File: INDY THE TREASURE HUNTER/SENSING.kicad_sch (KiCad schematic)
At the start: 1 part

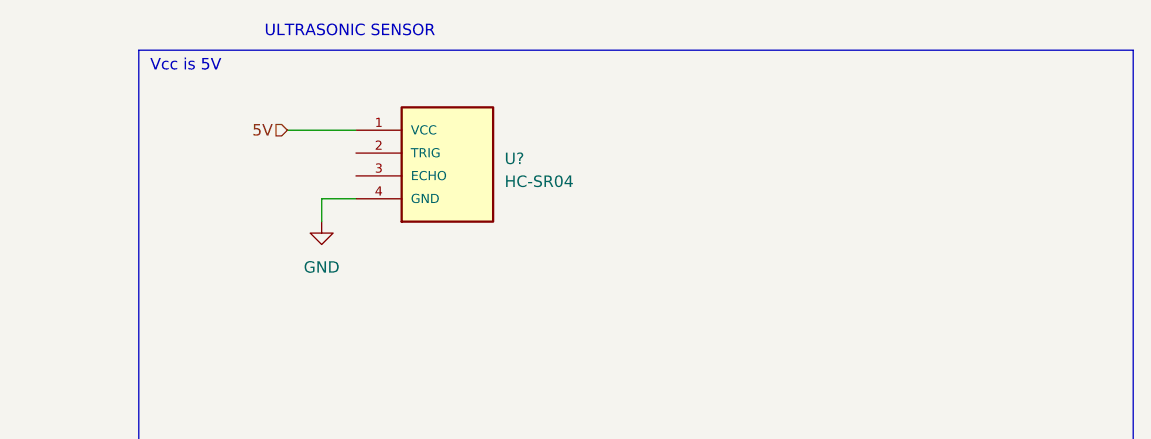
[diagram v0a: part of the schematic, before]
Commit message: 19:16
Got rid of the boxes around the logic level converters, we can neaten those up later it was just becoming a nightmare.

Also IMPORTANT:
Try to stick with this naming convention for logic level lines: NAMEOFLINE_VOLTAGE (eg: ULTRA_TRIG_3V3) so we can track the logic level voltages
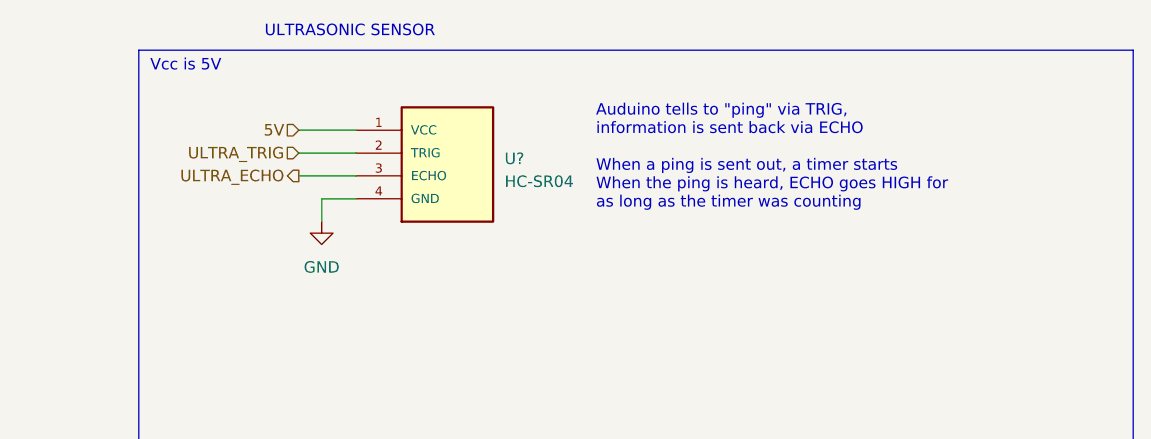
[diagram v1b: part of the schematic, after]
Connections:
- net ULTRA_TRIG: now reaches U?.2 (TRIG)
- net ULTRA_ECHO: now reaches U?.3 (ECHO)
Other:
- note added: "Auduino tells to "ping" via TRIG, information is sent back via ECHO When a ping is sent out, a timer starts When the ping is heard, ECHO goes HIGH for as long as the timer was counting"
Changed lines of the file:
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@@
 (kicad_sch (version 20230121) (generator eeschema)
   (paper "A4")
-  (wire (pts (xy 182.88 49.53) (xy 190.5 49.53))
+  (wire (pts (xy 184.15 54.61) (xy 190.5 54.61))
     (stroke (width 0) (type default))
   )
   (wire (pts (xy 190.5 57.15) (xy 186.69 57.15))
+    (stroke (width 0) (type default))
+  )
+  (wire (pts (xy 184.15 52.07) (xy 190.5 52.07))
+    (stroke (width 0) (type default))
+  )
+  (wire (pts (xy 184.15 49.53) (xy 190.5 49.53))
     (stroke (width 0) (type default))
   )
@@
     (effects (font (size 1.27 1.27)) (justify left bottom))
   )
-  (hierarchical_label "5V" (shape input) (at 182.88 49.53 180) (fields_autoplaced)
+  (text "Auduino tells to \"ping\" via TRIG,\ninformation is sent back via ECHO\n\nWhen a ping is sent out, a timer starts\nWhen the ping is heard, ECHO goes HIGH for\nas long as the timer was counting"
+    (at 217.17 58.42 0)
+    (effects (font (size 1.27 1.27)) (justify left bottom))
+  )
+  (hierarchical_label "5V" (shape input) (at 184.15 49.53 180) (fields_autoplaced)
     (effects (font (size 1.27 1.27)) (justify right))
   )
+  (hierarchical_label "ULTRA_ECHO" (shape output) (at 184.15 54.61 180) (fields_autoplaced)
+    (effects (font (size 1.27 1.27)) (justify right))
+  )
+  (hierarchical_label "ULTRA_TRIG" (shape input) (at 184.15 52.07 180) (fields_autoplaced)
+    (effects (font (size 1.27 1.27)) (justify right))
+  )

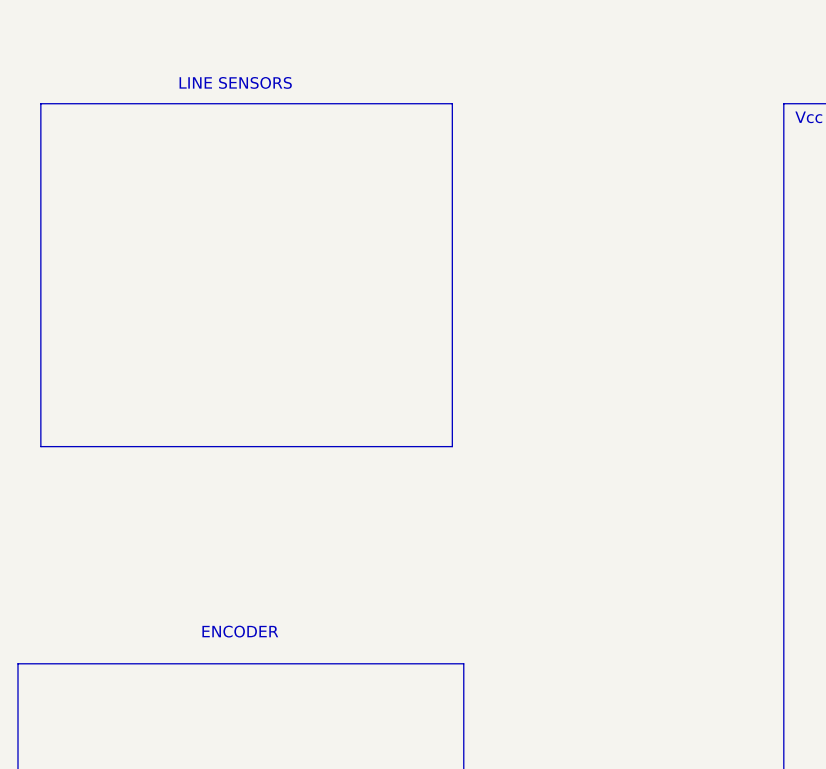
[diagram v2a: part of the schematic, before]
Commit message: Line sensor data lines configured
Im pretty sure the line sensors operate fine on 3v3, so no need to shift their logic levels or anything
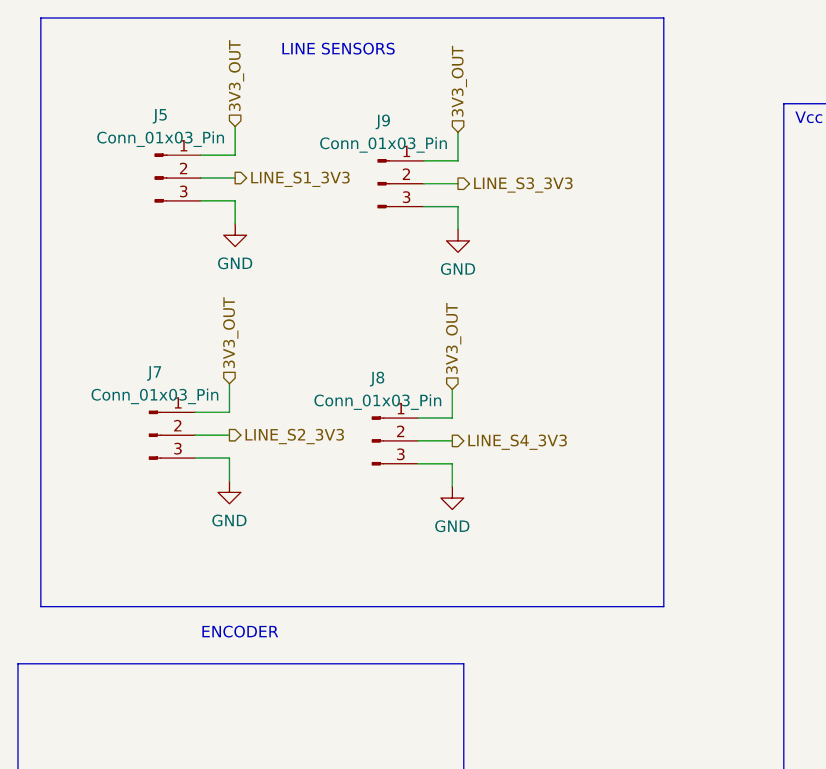
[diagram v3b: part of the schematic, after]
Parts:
- added J5, J7, J8, J9: Conn_01x03_Pin, symbol Connector:Conn_01x03_Pin
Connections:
- net GND: now also J5.3 (Pin_3), J7.3 (Pin_3), J8.3 (Pin_3), J9.3 (Pin_3)
- new net 3V3_OUT: J5.1 (Pin_1), J7.1 (Pin_1), J8.1 (Pin_1), J9.1 (Pin_1)
- new net LINE_S1_3V3: J5.2 (Pin_2)
- new net LINE_S2_3V3: J7.2 (Pin_2)
- new net LINE_S3_3V3: J9.2 (Pin_2)
- new net LINE_S4_3V3: J8.2 (Pin_2)

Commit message: I think thats that?
There are a few things that remain unclear. For milestone 1's handin, it should be ok, just some cleanup in the morning might be necessary and group discussion on how to do things
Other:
- note added: "No instruction given on how to use this Research later, I suppose"
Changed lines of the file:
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@@
+    (effects (font (size 1.27 1.27)) (justify left bottom))
+  )
+  (text "No instruction given on how to use this\nResearch later, I suppose"
+    (at 85.725 108.585 0)
     (effects (font (size 1.27 1.27)) (justify left bottom))
   )

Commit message: Neatened up schematic for milestone 1 handin
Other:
- moved on the sheet: J5, J7, J8, J9, U?
